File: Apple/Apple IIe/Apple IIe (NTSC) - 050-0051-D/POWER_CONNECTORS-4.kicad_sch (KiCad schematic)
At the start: 36 parts, among them J0 Conn_02x30_Counter_Clockwise, J1 Conn_02x25_Counter_Clockwise, J14 Conn_01x06, J15 Conn_02x08_Counter_Clockwise, J16 Conn_01x11, J17 Conn_02x13_Odd_Even, J2 Conn_02x25_Counter_Clockwise, J20 Conn_01x04, J3 Conn_02x25_Counter_Clockwise, J4 Conn_02x25_Counter_Clockwise, J5 Conn_02x25_Counter_Clockwise, J6 Conn_02x25_Counter_Clockwise, J7 Conn_02x25_Counter_Clockwise, J8 DB9_Female, X7 SolderJumper_2_Open

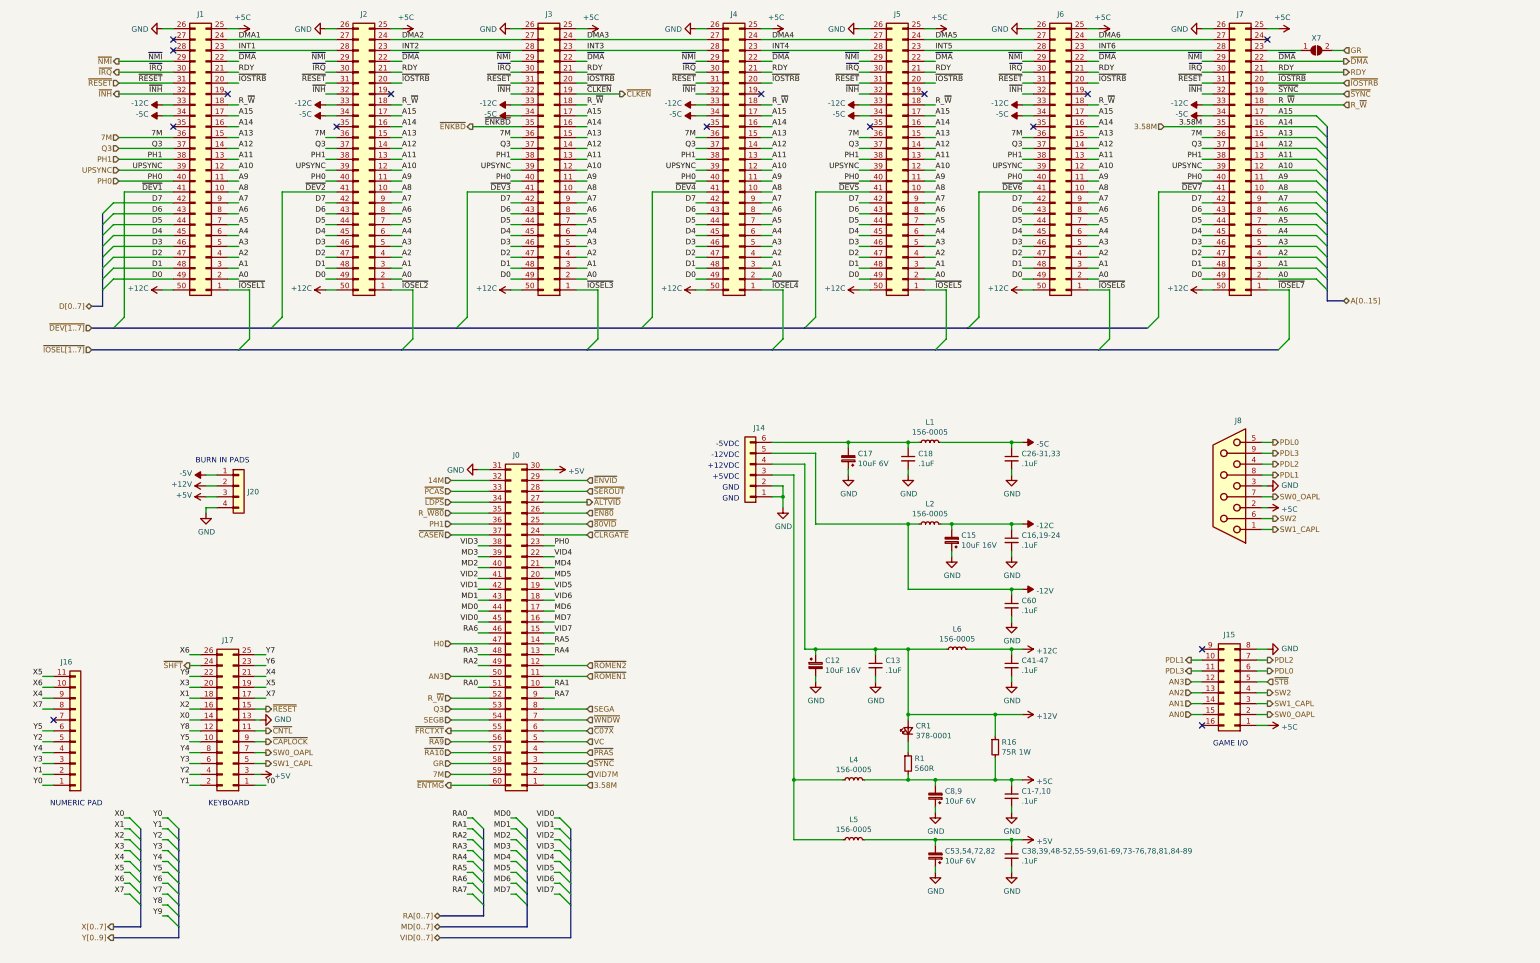
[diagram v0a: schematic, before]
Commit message: Updated symbols, added power symbols for multi-units, and passed ERC!
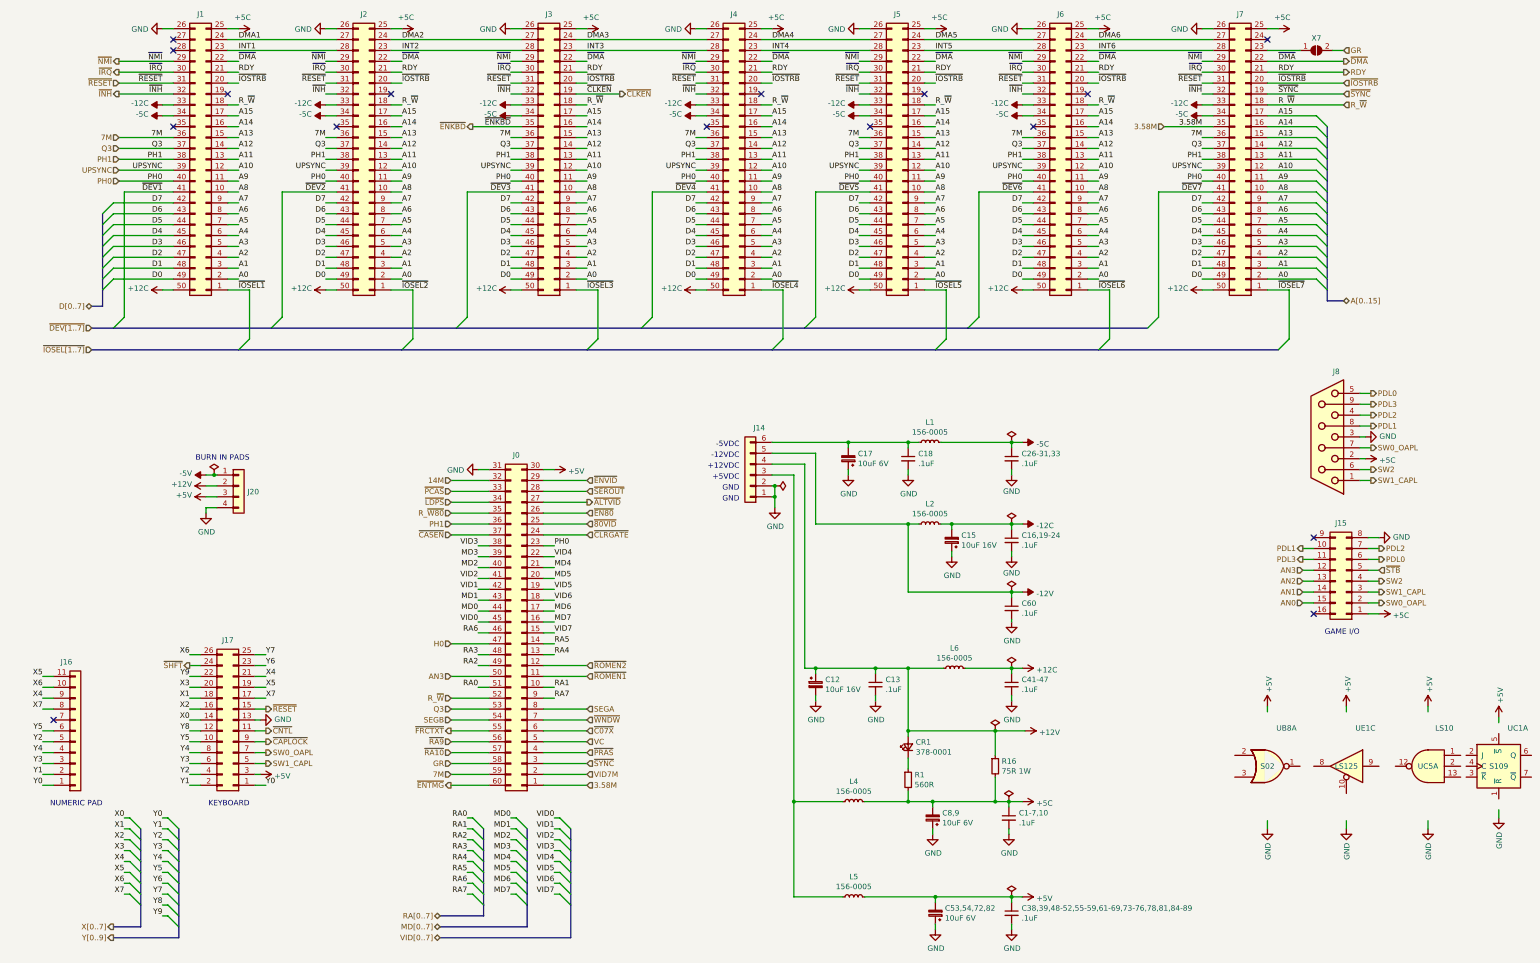
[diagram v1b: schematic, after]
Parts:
- added UB8: S02, symbol 74xx:7402
- added UC1: S109, symbol 74xx:74LS109
- added UC5: LS10, symbol 74xx:74LS10
- added UE1: LS125, symbol 74xx:74LS125
- C12, C15, C17, C53,54,72,82, C8,9: symbol Device:CP_Small -> Device:C_Polarized_Small
- J8: symbol Connector:DB9_Female -> Connector:DE9_Receptacle
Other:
- moved on the sheet: C1-7,10, C12, C13, C38,39,48-52,55-59,61-69,73-76,78,81,84-89, C41-47, C53,54,72,82, C60, C8,9, CR1, J15, J8, L4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
